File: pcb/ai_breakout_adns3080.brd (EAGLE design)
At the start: 38.1 x 25.4 mm, 24 parts, among them J1 1X10, U1 VREG-MIC5205-3.3, U2 ADNS-3080, X1 RESON

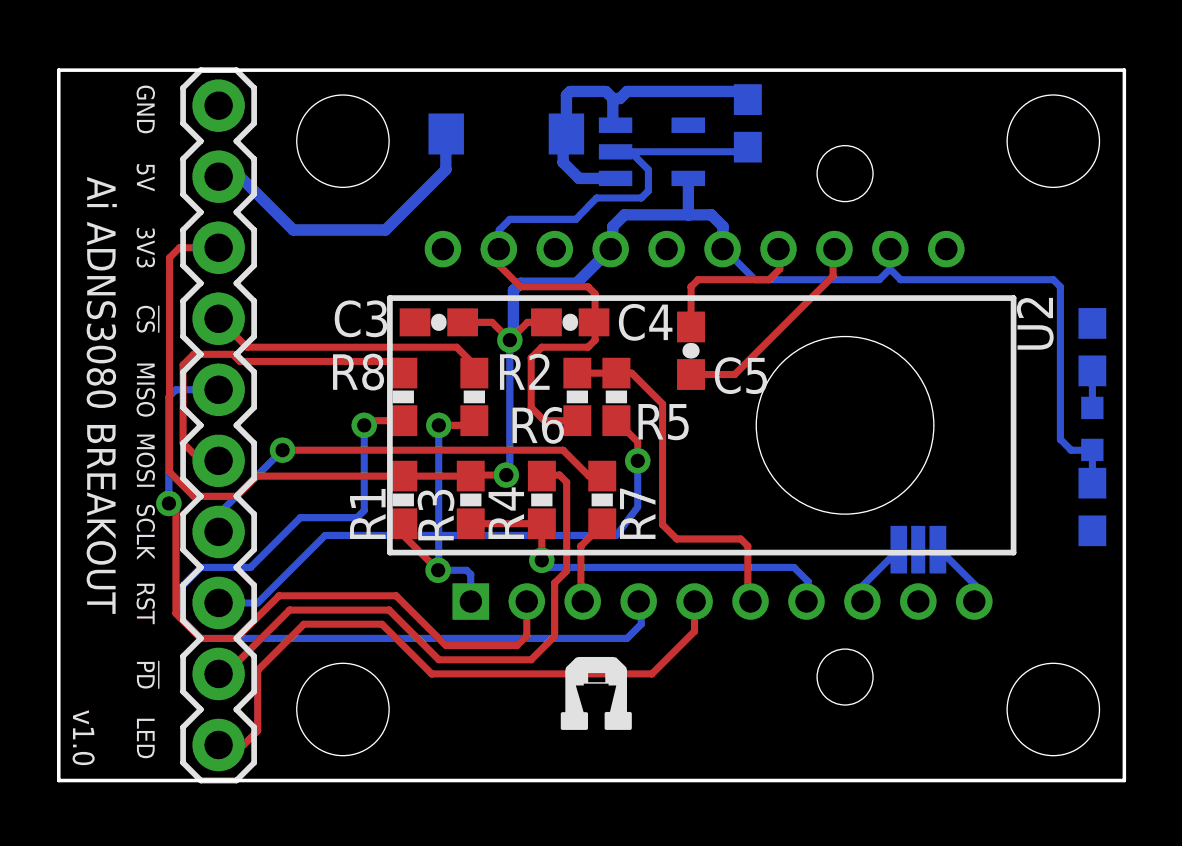
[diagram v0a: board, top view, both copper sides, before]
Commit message: Revised version.  Finished BOM.
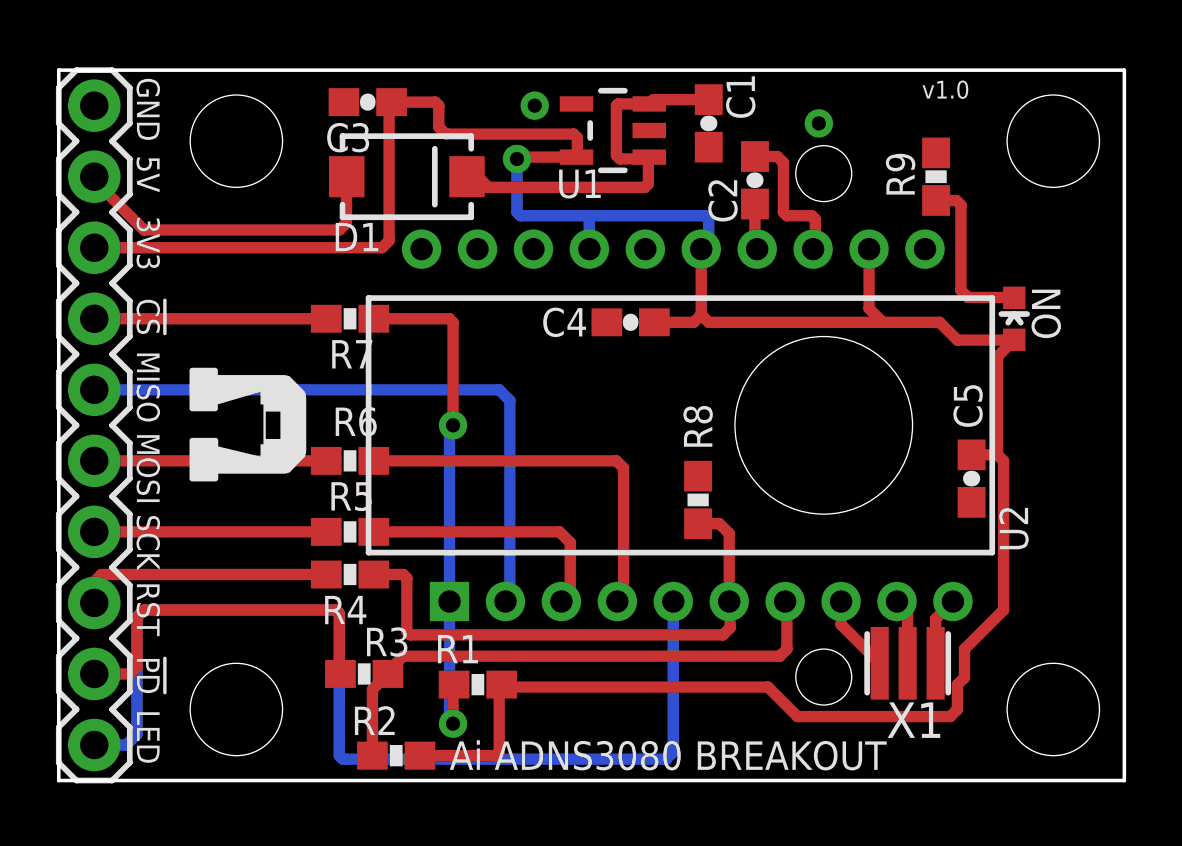
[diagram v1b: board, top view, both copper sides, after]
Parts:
- added U$2, U$3: AI-LOGOM, Ai_Miscellany:AI-LOGO-M
- C1, C3, C4: device Ai_Passives:0603-CAP -> Ai_Passives:CAP-0603
- C2: value 1uF -> 2.2uF; device Ai_Passives:0603-CAP -> Ai_Passives:CAP-0603
- C5: value 2.2uF -> 1uF; device Ai_Passives:0603-CAP -> Ai_Passives:CAP-0603
- D1: value DIODE -> DIODESMA-403D
- ON: value RED -> BLUE; device Ai_LED:0603-LED -> Ai_LED:LED-0603
- R1, R7: device Ai_Passives:0603-RES -> Ai_Passives:RES-0603
- R2, R8: value 1K -> 20K; device Ai_Passives:0603-RES -> Ai_Passives:RES-0603
- R3: value 20K -> 10K; device Ai_Passives:0603-RES -> Ai_Passives:RES-0603
- R4, R5: value 10K -> 1K; device Ai_Passives:0603-RES -> Ai_Passives:RES-0603
- R6: value 20K -> 1K; device Ai_Passives:0603-RES -> Ai_Passives:RES-0603
- R9: value 330 -> 1K; device Ai_Passives:0603-RES -> Ai_Passives:RES-0603
- U1: value VREG-MIC5205-3.3 -> MIC5205-3.3
- X1: value RESON -> RESON025X020; device Ai_Passives:RESON-SMD -> Ai_Passives:RESON-SMD-025X020
- moved C2 16.8 mm to (24.9, 21.5), flipped to the top
- moved R2 13.1 mm to (12.1, 0.89), turned to 0 degrees
- moved R8 11.2 mm to (22.9, 10.0)
- moved R7 11.1 mm to (10.4, 16.5), turned to 0 degrees
- moved C5 11.0 mm to (32.6, 10.8), turned to 270 degrees
- moved R5 10.7 mm to (10.4, 8.89), turned to 0 degrees
- moved R6 8.44 mm to (10.4, 11.4), turned to 0 degrees
- moved C3 8.27 mm to (11.0, 24.3)
- moved R9 8.27 mm to (31.4, 21.6), flipped to the top
- moved R4 7.36 mm to (10.4, 7.37), turned to 180 degrees
- moved R3 7.30 mm to (10.9, 3.81), turned to 180 degrees
- moved R1 7.12 mm to (15.0, 3.43), turned to 180 degrees
- moved ON 4.83 mm to (34.2, 16.5), flipped to the top
- moved J1 4.45 mm to (1.27, 12.7)
- moved X1 4.08 mm to (30.4, 4.19), flipped to the top, turned to 180 degrees
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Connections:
- removed net N$14: R1.2, R2.2, U2.1
- removed net N$18: R3.1, R4.1, U2.7
- removed net SCLK: J1.4, R7.1
- new net N$2: U2.9, X1.2
- new net N$4: R1.2, R7.2, U2.1
- new net N$7: R2.1, R3.1, U2.7
- new net SCK: J1.4, R5.1
- net !CS: now also R7.1; no longer R2.1
- net !PD: now also R3.2; no longer R4.2
- net 3V3: now also C5.1, R2.2; no longer C2.1, R3.2
- net GND: now also C5.2, R8.1; no longer C2.2, R6.1, U2.9, X1.2
- net MOSI: now also R6.1; no longer R8.1
- net N$10: now also R6.2; no longer R8.2
- net N$12: now also R4.1, R8.2; no longer R5.1, R6.2
- net N$16: now also C2.1; no longer C5.1
- net N$17: now also C2.2; no longer C5.2
- net N$5: now also R5.2; no longer R7.2
- net RST: now also R4.2; no longer R5.2
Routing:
- net 3V3: track 65.6 -> 93.5 mm, vias 2 -> 1
- net GND: track 25.9 -> 0.00 mm, vias 0 -> 2
- net N$7: track 0.00 -> 19.6 mm
- net N$4: track 0.00 -> 18.8 mm, vias 0 -> 2
- net N$10: track 31.2 -> 13.9 mm, vias 1 -> 0
- net SCLK: track 15.7 -> 0.00 mm, vias 1 -> 0
- net N$18: track 14.4 -> 0.00 mm, vias 1 -> 0
- net LEDCTRL: track 22.5 -> 35.8 mm
- net N$14: track 10.9 -> 0.00 mm, vias 2 -> 0
- net RST: track 19.9 -> 9.16 mm, vias 1 -> 0
- net SCK: track 0.00 -> 8.29 mm
- net !PD: track 20.9 -> 13.0 mm
- net N$5: track 3.13 -> 9.42 mm
- net N$12: track 13.2 -> 19.5 mm
- net N$26: track 1.32 -> 6.02 mm
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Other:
- board text added: "Designed in Pasadena, CA."
- board text added: "SCK"
- board text added: "VDD"
- board text added: "http://acrobotic.com/ADNS3080"
- board text removed: "/home/xisco/ai_logo.bmp"
- board text removed: "SCLK"

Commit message: updating to use the latest libraries
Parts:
- D1: value DIODESMA-403D -> (none)
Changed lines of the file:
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@@
 <layer number="111" name="circles" color="7" fill="1" visible="no" active="yes"/>
 <layer number="112" name="hoeken" color="7" fill="1" visible="no" active="yes"/>
+<layer number="113" name="Route13" color="7" fill="1" visible="no" active="no"/>
 <layer number="116" name="Patch_BOT" color="9" fill="4" visible="no" active="yes"/>
+<layer number="117" name="mPads" color="7" fill="1" visible="no" active="no"/>
+<layer number="118" name="mVias" color="7" fill="1" visible="no" active="no"/>
+<layer number="119" name="mUnrouted" color="7" fill="1" visible="no" active="no"/>
+<layer number="120" name="mDimension" color="7" fill="1" visible="no" active="no"/>
 <layer number="121" name="_tsilk" color="7" fill="1" visible="no" active="yes"/>
 <layer number="122" name="_bsilk" color="7" fill="1" visible="no" active="yes"/>
@@
 <layer number="127" name="_tValues" color="7" fill="1" visible="yes" active="yes"/>
 <layer number="128" name="_bValues" color="7" fill="1" visible="yes" active="yes"/>
+<layer number="129" name="mtStop" color="7" fill="1" visible="no" active="no"/>
+<layer number="130" name="mbStop" color="7" fill="1" visible="no" active="no"/>
 <layer number="131" name="tAdjust" color="7" fill="1" visible="yes" active="yes"/>
 <layer number="132" name="bAdjust" color="7" fill="1" visible="yes" active="yes"/>
+<layer number="133" name="mtFinish" color="7" fill="1" visible="no" active="no"/>
+<layer number="134" name="mbFinish" color="7" fill="1" visible="no" active="no"/>
+<layer number="135" name="mtGlue" color="7" fill="1" visible="no" active="no"/>
+<layer number="136" name="mbGlue" color="7" fill="1" visible="no" active="no"/>
+<layer number="137" name="mtTest" color="7" fill="1" visible="no" active="no"/>
+<layer number="138" name="mbTest" color="7" fill="1" visible="no" active="no"/>
+<layer number="139" name="mtKeepout" color="7" fill="1" visible="no" active="no"/>
+<layer number="140" name="mbKeepout" color="7" fill="1" visible="no" active="no"/>
+<layer number="141" name="mtRestrict" color="7" fill="1" visible="no" active="no"/>
+<layer number="142" name="mbRestrict" color="7" fill="1" visible="no" active="no"/>
+<layer number="143" name="mvRestrict" color="7" fill="1" visible="no" active="no"/>
 <layer number="144" name="Drill_legend" color="7" fill="1" visible="no" active="yes"/>
+<layer number="145" name="mHoles" color="7" fill="1" visible="no" active="no"/>
+<layer number="146" name="mMilling" color="7" fill="1" visible="no" active="no"/>
+<layer number="147" name="mMeasures" color="7" fill="1" visible="no" active="no"/>
+<layer number="148" name="mDocument" color="7" fill="1" visible="no" active="no"/>
+<layer number="149" name="mReference" color="7" fill="1" visible="no" active="no"/>
 <layer number="150" name="Notes" color="7" fill="1" visible="no" active="yes"/>
 <layer number="151" name="HeatSink" color="7" fill="1" visible="no" active="yes"/>
@@
 <layer number="154" name="FabDoc2" color="2" fill="1" visible="no" active="no"/>
 <layer number="155" name="FabDoc3" color="7" fill="15" visible="no" active="no"/>
+<layer number="191" name="mNets" color="7" fill="1" visible="no" active="no"/>
+<layer number="192" name="mBusses" color="7" fill="1" visible="no" active="no"/>
+<layer number="193" name="mPins" color="7" fill="1" visible="no" active="no"/>
+<layer number="194" name="mSymbols" color="7" fill="1" visible="no" active="no"/>
+<layer number="195" name="mNames" color="7" fill="1" visible="no" active="no"/>
+<layer number="196" name="mValues" color="7" fill="1" visible="no" active="no"/>
 <layer number="199" name="PSR2000 hulplijn" color="14" fill="1" visible="no" active="yes"/>
 <layer number="200" name="200bmp" color="1" fill="10" visible="no" active="no"/>
@@
 <element name="STANDOFF4" library="Ai_Electromechanical" package="STAND-OFF" value="STAND-OFF" x="35.56" y="2.54"/>
 <element name="J1" library="Ai_Connectors" package="1X10" value="1X10" x="1.27" y="12.7" smashed="yes" rot="R90"/>
-<element name="D1" library="Ai_DiscreteSemis" package="SMA-403D" value="DIODESMA-403D" x="12.446" y="21.59" smashed="yes">
+<element name="D1" library="Ai_DiscreteSemis" package="SMA-403D" value="" x="12.446" y="21.59" smashed="yes">
 <attribute name="NAME" x="9.779" y="18.923" size="1.016" layer="25" ratio="15"/>
 </element>
